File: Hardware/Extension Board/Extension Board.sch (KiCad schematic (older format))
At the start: 32 parts, among them J1 ARDUINO_COMMS, J10 CNX_MODE, J11 CNX_TUNING, J12 CNX_I2C, J13 CNX_I2C, J14 CNX_SPI, J15 CNX_SD, J16 CNX_TFT, J2 ARDUINO_DIGITAL, J3 ARDUINO_ANALOG, J4 CNX_LED, J5 CNX_LED, J6 CNX_LED, J7 CNX_LED, J8 CNX_SPARE, J9 CNX_NEXT_AGAIN, U1 74HC14

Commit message: PCB pour Extension board
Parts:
- removed J1: ARDUINO_COMMS, Connector_PinHeader_2.54mm:PinHeader_1x08_P2.54mm_Vertical, symbol Connector_Generic:Conn_01x08
- removed RN1: 10k, Resistor_THT:R_Array_SIP9, symbol Device:R_Network08
- added H1, H2: MountingHole, MountingHole:MountingHole_3.2mm_M3, symbol Mechanical:MountingHole
- added J7: ARDUINO_COMMS, Connector_PinHeader_2.54mm:PinHeader_1x06_P2.54mm_Vertical, symbol Connector_Generic:Conn_01x06
- added RN1: 10k, Resistor_THT:R_Array_SIP5, symbol Device:R_Network04
- C1, C2: footprint (none) -> Capacitor_THT:C_Rect_L7.2mm_W2.5mm_P5.00mm_FKS2_FKP2_MKS2_MKP2
- J1: renamed from J7; footprint MesModules:Bloc_de_jonction_CI-MPT_2.54mm_01x02 -> Connector_JST:JST_XH_B2B-XH-A_1x02_P2.50mm_Vertical
- J10, J12, J13: footprint Connector_JST:JST_EH_B4B-EH-A_1x04_P2.50mm_Vertical -> Connector_JST:JST_XH_B4B-XH-A_1x04_P2.50mm_Vertical
- J11, J9: footprint Connector_JST:JST_EH_B3B-EH-A_1x03_P2.50mm_Vertical -> Connector_JST:JST_XH_B3B-XH-A_1x03_P2.50mm_Vertical
- J14: footprint Connector_JST:JST_EH_B6B-EH-A_1x06_P2.50mm_Vertical -> Connector_JST:JST_XH_B6B-XH-AM_1x06_P2.50mm_Vertical
- J15: footprint Connector_JST:JST_EH_B4B-EH-A_1x04_P2.50mm_Vertical -> Connector_JST:JST_XH_B4B-XH-AM_1x04_P2.50mm_Vertical
- J16: footprint Connector_JST:JST_EH_B8B-EH-A_1x08_P2.50mm_Vertical -> Connector_JST:JST_XH_B8B-XH-AM_1x08_P2.50mm_Vertical
- J2: renamed from J6; footprint MesModules:Bloc_de_jonction_CI-MPT_2.54mm_01x02 -> Connector_JST:JST_XH_B2B-XH-A_1x02_P2.50mm_Vertical
- J3: renamed from J5; footprint MesModules:Bloc_de_jonction_CI-MPT_2.54mm_01x02 -> Connector_JST:JST_XH_B2B-XH-A_1x02_P2.50mm_Vertical
- J4: footprint MesModules:Bloc_de_jonction_CI-MPT_2.54mm_01x02 -> Connector_JST:JST_XH_B2B-XH-A_1x02_P2.50mm_Vertical
- J5: renamed from J8; footprint MesModules:Bloc_de_jonction_CI-MPT_2.54mm_01x03 -> Connector_JST:JST_XH_B3B-XH-A_1x03_P2.50mm_Vertical
- R1, R2, R3, R4, R5: value 220 -> 200; footprint (none) -> Resistor_THT:R_Axial_DIN0207_L6.3mm_D2.5mm_P10.16mm_Horizontal
- R10: value 20k -> 90k; footprint (none) -> Resistor_THT:R_Axial_DIN0207_L6.3mm_D2.5mm_P10.16mm_Horizontal
- R6: value 1M -> A CALCULER; footprint (none) -> Resistor_THT:R_Axial_DIN0411_L9.9mm_D3.6mm_P20.32mm_Horizontal
- R7, R8: footprint (none) -> Resistor_THT:R_Axial_DIN0207_L6.3mm_D2.5mm_P10.16mm_Horizontal
- R9: value 10k -> 50k; footprint (none) -> Resistor_THT:R_Axial_DIN0207_L6.3mm_D2.5mm_P10.16mm_Horizontal
- renumbered J2 to J6, J3 to J8
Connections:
- net labels added: D16, D17, D29, D31, D33, D40, D42, D48
- net labels removed: D27, D35, D41, D43, D49
- wire segments 154 -> 157
- no-connect marks 31 -> 25
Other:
- note added: "INPUTS\nwith ISR"
- note added: "PWM\nOUTPUTS"
- moved on the sheet: J13, J2, J4, J5, J8, R1, R2, R3, R4, R5

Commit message: PCB Extension board
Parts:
- J10: value CNX_MODE -> MODE
- J11: value CNX_TUNING -> TUNING
- J12, J13: value CNX_I2C -> I2C
- J14: value CNX_SPI -> SPI
- J15: value CNX_SD -> SD
- J16: value CNX_TFT -> TFT
- J5: value CNX_SPARE -> SPARE
- J9: value CNX_NEXT_AGAIN -> NEXT_AGAIN
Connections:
- net D18: now also U1.4; no longer U1.2
- net D19: now also U1.2; no longer U1.4
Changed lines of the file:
@@
 P 10400 1100
 F 0 "J11" H 10650 1000 50  0000 R CNN
-F 1 "CNX_TUNING" H 10950 1100 50  0000 R CNN
+F 1 "TUNING" H 10750 1100 50  0000 R CNN
 F 2 "Connector_JST:JST_XH_B3B-XH-A_1x03_P2.50mm_Vertical" H 10400 1100 50  0001 C CNN
 F 3 "~" H 10400 1100 50  0001 C CNN
@@
 P 6500 4250
 F 0 "J5" V 6750 4200 50  0000 L CNN
-F 1 "CNX_SPARE" V 6650 4050 50  0000 L CNN
+F 1 "SPARE" V 6650 4150 50  0000 L CNN
 F 2 "Connector_JST:JST_XH_B3B-XH-A_1x03_P2.50mm_Vertical" H 6500 4250 50  0001 C CNN
 F 3 "~" H 6500 4250 50  0001 C CNN
@@
 P 10150 2950
 F 0 "J13" H 10250 2750 50  0000 L CNN
-F 1 "CNX_I2C" H 10230 2851 50  0000 L CNN
+F 1 "I2C" H 10230 2851 50  0000 L CNN
 F 2 "Connector_JST:JST_XH_B4B-XH-A_1x04_P2.50mm_Vertical" H 10150 2950 50  0001 C CNN
 F 3 "~" H 10150 2950 50  0001 C CNN
@@
 Text GLabel 2550 3100 2    50   Input ~ 0
 D25
+Text GLabel 3650 5950 0    50   Input ~ 0
+D18
 Text GLabel 3650 5600 0    50   Input ~ 0
-D18
-Text GLabel 3650 5950 0    50   Input ~ 0
 D19
 Wire Wire Line
@@
 P 10150 4000
 F 0 "J14" H 10250 3700 50  0000 L CNN
-F 1 "CNX_SPI" H 10250 3800 50  0000 L CNN
+F 1 "SPI" H 10250 3800 50  0000 L CNN
 F 2 "Connector_JST:JST_XH_B6B-XH-AM_1x06_P2.50mm_Vertical" H 10150 4000 50  0001 C CNN
 F 3 "~" H 10150 4000 50  0001 C CNN
@@
 P 6800 5700
 F 0 "J9" H 6900 5700 50  0000 L CNN
-F 1 "CNX_NEXT_AGAIN" H 6900 5600 50  0000 L CNN
+F 1 "NEXT_AGAIN" H 6900 5600 50  0000 L CNN
 F 2 "Connector_JST:JST_XH_B3B-XH-A_1x03_P2.50mm_Vertical" H 6800 5700 50  0001 C CNN
 F 3 "~" H 6800 5700 50  0001 C CNN
@@
 P 8750 2950
 F 0 "J12" H 8850 2750 50  0000 L CNN
-F 1 "CNX_I2C" H 8830 2851 50  0000 L CNN
+F 1 "I2C" H 8830 2851 50  0000 L CNN
 F 2 "Connector_JST:JST_XH_B4B-XH-A_1x04_P2.50mm_Vertical" H 8750 2950 50  0001 C CNN
 F 3 "~" H 8750 2950 50  0001 C CNN
@@
 P 10350 5100
 F 0 "J15" H 10450 4900 50  0000 L CNN
-F 1 "CNX_SD" H 10430 5001 50  0000 L CNN
+F 1 "SD" H 10430 5001 50  0000 L CNN
 F 2 "Connector_JST:JST_XH_B4B-XH-AM_1x04_P2.50mm_Vertical" H 10350 5100 50  0001 C CNN
 F 3 "~" H 10350 5100 50  0001 C CNN
@@
 P 10350 5850
 F 0 "J16" H 10450 5450 50  0000 L CNN
-F 1 "CNX_TFT" H 10450 5550 50  0000 L CNN
+F 1 "TFT" H 10450 5550 50  0000 L CNN
 F 2 "Connector_JST:JST_XH_B8B-XH-AM_1x08_P2.50mm_Vertical" H 10350 5850 50  0001 C CNN
 F 3 "~" H 10350 5850 50  0001 C CNN
@@
 P 6350 1950
 F 0 "J10" H 6550 1750 50  0000 R CNN
-F 1 "CNX_MODE" H 6800 1850 50  0000 R CNN
+F 1 "MODE" H 6650 1850 50  0000 R CNN
 F 2 "Connector_JST:JST_XH_B4B-XH-A_1x04_P2.50mm_Vertical" H 6350 1950 50  0001 C CNN
 F 3 "~" H 6350 1950 50  0001 C CNN
@@
 P 1850 6200
 F 0 "J7" V 1814 6480 50  0000 L CNN
-F 1 "ARDUINO_COMMS" V 1723 6480 50  0000 L CNN
+F 1 "ARDUINO_COMMS" V 1950 5850 50  0000 L CNN
 F 2 "Connector_PinHeader_2.54mm:PinHeader_1x06_P2.54mm_Vertical" H 1850 6200 50  0001 C CNN
 F 3 "~" H 1850 6200 50  0001 C CNN

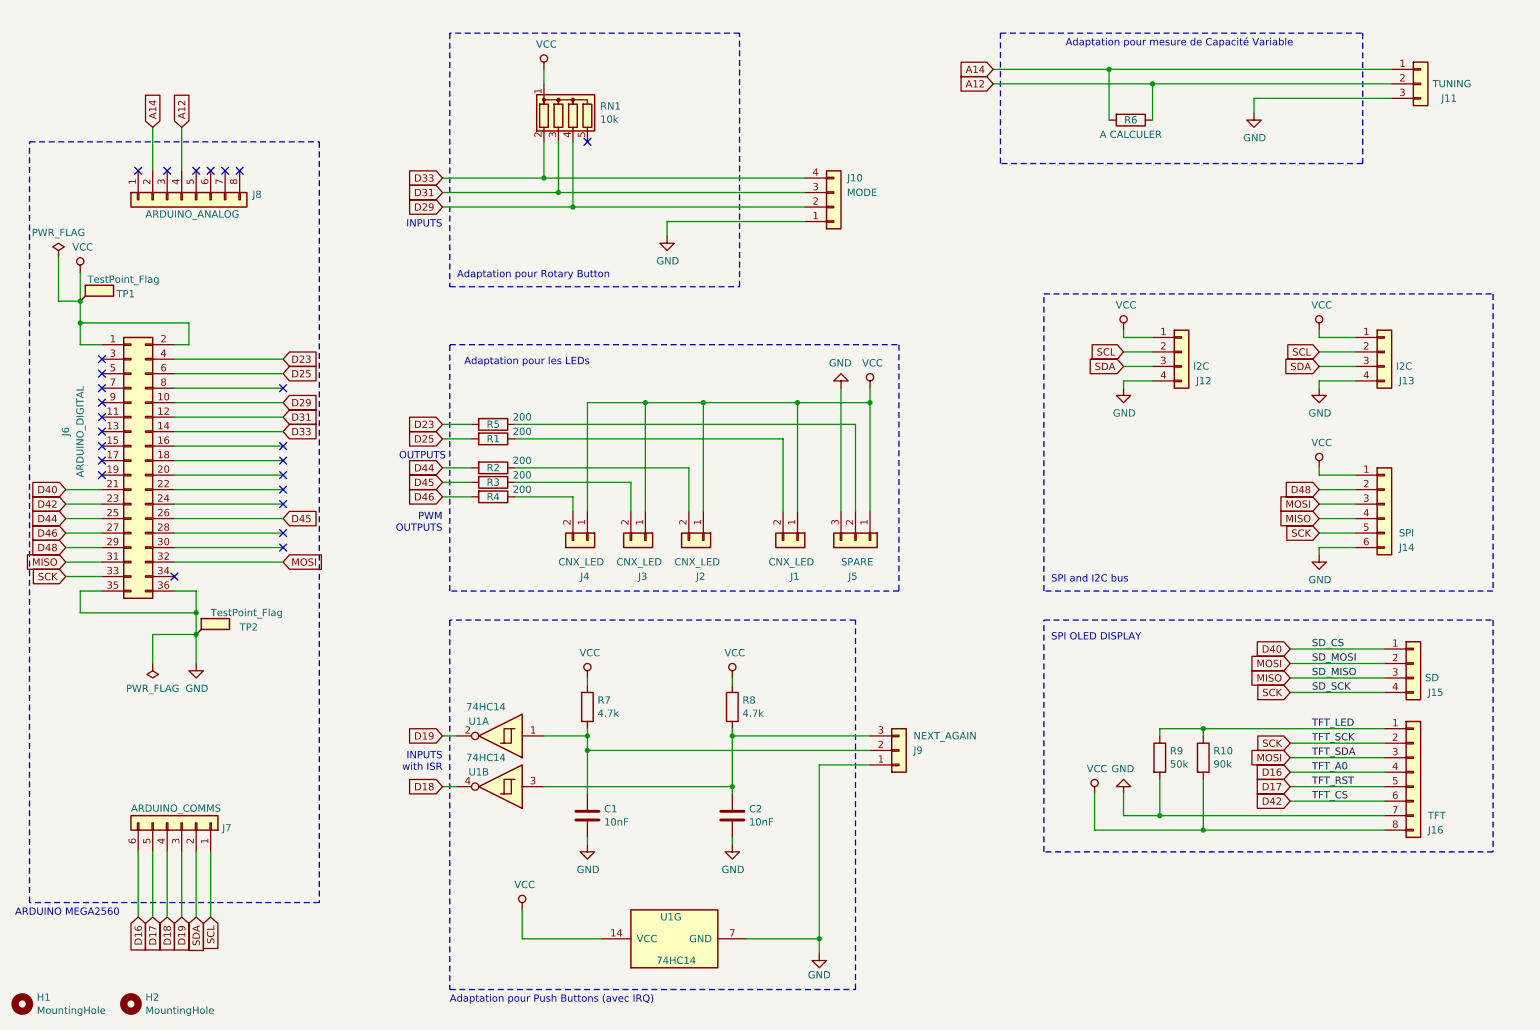
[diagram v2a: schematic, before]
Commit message: PCB Layout complete
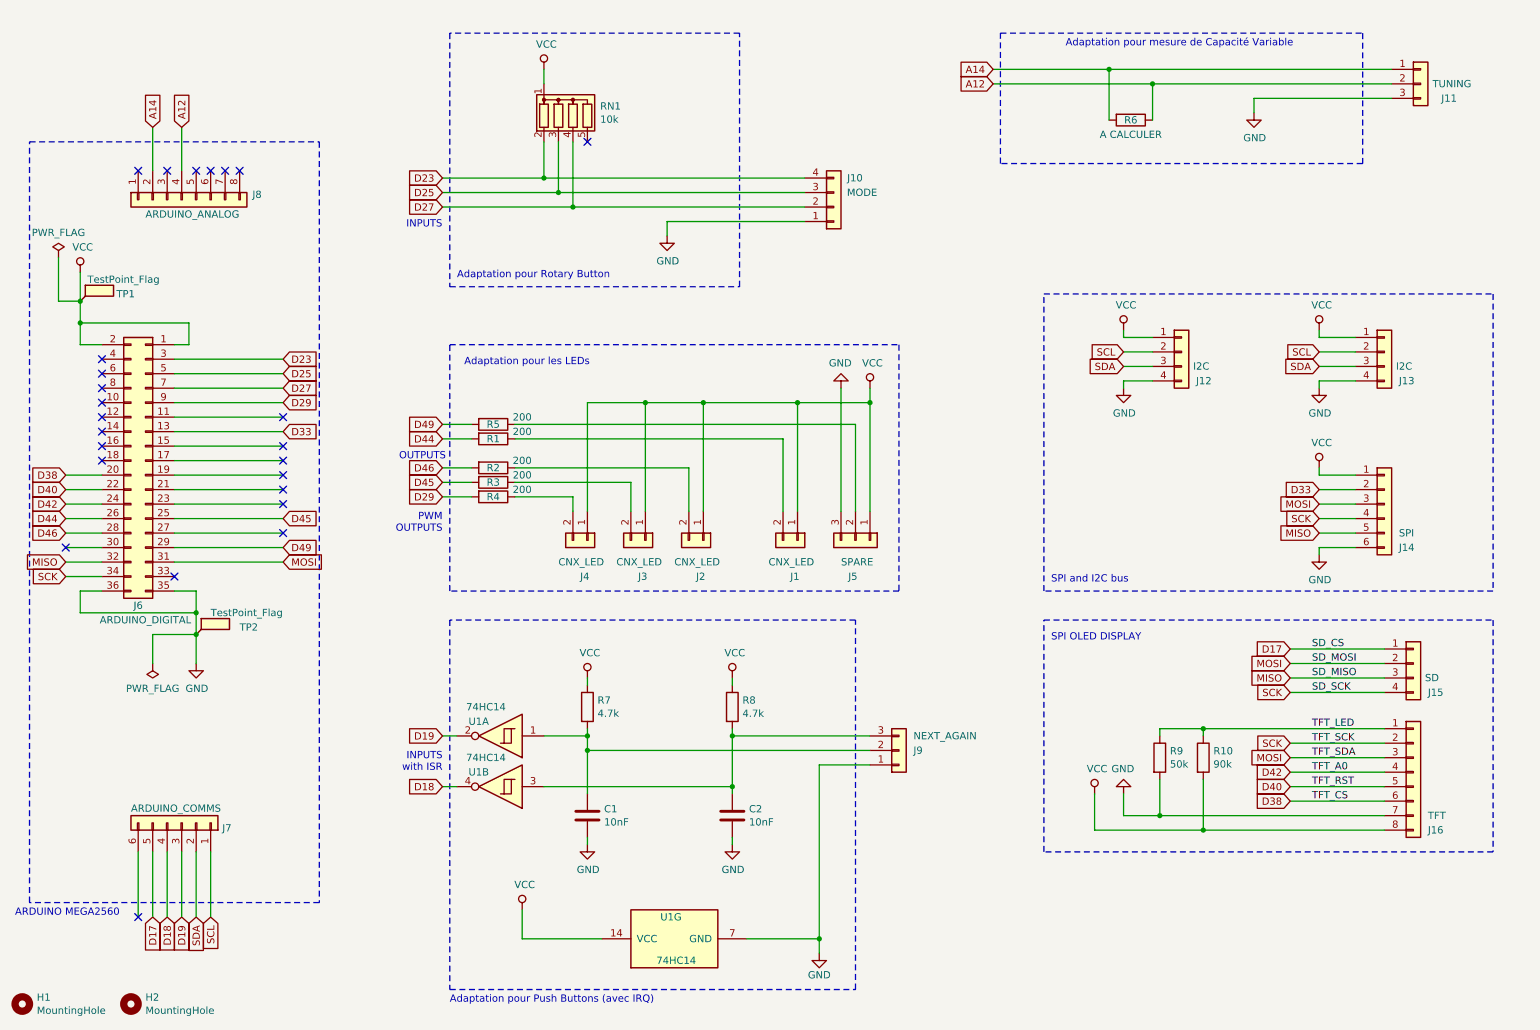
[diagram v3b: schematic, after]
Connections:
- net D17: now also J15.1 (Pin_1); no longer J16.5 (Pin_5)
- net D23: now also J10.4 (Pin_4), J6.3 (Pin_3), RN1.2 (R1); no longer J6.4 (Pin_4), R5.2
- net D25: now also J10.3 (Pin_3), J6.5 (Pin_5), RN1.3 (R2); no longer J6.6 (Pin_6), R1.2
- net D29: now also J6.9 (Pin_9), R4.2; no longer J10.2 (Pin_2), J6.10 (Pin_10), RN1.4 (R3)
- net D33: now also J14.2 (Pin_2), J6.13 (Pin_13); no longer J10.4 (Pin_4), J6.14 (Pin_14), RN1.2 (R1)
- net D40: now also J16.5 (Pin_5), J6.22 (Pin_22); no longer J15.1 (Pin_1), J6.21 (Pin_21)
- net D42: now also J16.4 (Pin_4), J6.24 (Pin_24); no longer J16.6 (Pin_6), J6.23 (Pin_23)
- net D44: now also J6.26 (Pin_26), R1.2; no longer J6.25 (Pin_25), R2.2
- net D45: now also J6.25 (Pin_25); no longer J6.26 (Pin_26)
- net D46: now also J6.28 (Pin_28), R2.2; no longer J6.27 (Pin_27), R4.2
- net MISO: now also J14.5 (Pin_5), J6.32 (Pin_32); no longer J14.4 (Pin_4), J6.31 (Pin_31)
- net MOSI: now also J6.31 (Pin_31); no longer J6.32 (Pin_32)
- net SCK: now also J14.4 (Pin_4), J6.34 (Pin_34); no longer J14.5 (Pin_5), J6.33 (Pin_33)
- net D38: now reaches J6.20 (Pin_20)
- net D38: now also J16.6 (Pin_6)
- net D27: now reaches J6.7 (Pin_7)
- net D27: now also J10.2 (Pin_2), RN1.4 (R3)
- net D16: no longer names the net of J7.6 (Pin_6)
- net D16: no longer J16.4 (Pin_4)
- removed net D31: J10.3 (Pin_3), J6.12 (Pin_12), RN1.3 (R2)
- net D48 renamed D49
- net D49: now also R5.2; no longer J14.2 (Pin_2)
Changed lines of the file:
@@
 	1800 4400 2550 4400
-Wire Wire Line
-	1050 4400 1300 4400
-Wire Wire Line
-	1050 4500 1300 4500
 Wire Wire Line
 	1950 4600 1800 4600
@@
 Wire Wire Line
 	1850 1700 1850 1400
-Text GLabel 9700 4100 0    50   Input ~ 0
+Text GLabel 9700 4200 0    50   Input ~ 0
 MISO
 Text GLabel 9700 4000 0    50   Input ~ 0
 MOSI
-Text GLabel 9700 4200 0    50   Input ~ 0
+Text GLabel 9700 4100 0    50   Input ~ 0
 SCK
 Wire Wire Line
@@
 	0    -1   -1   0
 $EndComp
-Text GLabel 2550 3000 2    50   Input ~ 0
-D23
-Text GLabel 2550 3100 2    50   Input ~ 0
-D25
+Text GLabel 2550 4300 2    50   Input ~ 0
+D49
+Text GLabel 2550 3500 2    50   Input ~ 0
+D33
 Text GLabel 3650 5950 0    50   Input ~ 0
 D18
@@
 	1    0    0    -1
 $EndComp
-Text GLabel 9700 3900 0    50   Input ~ 0
-D48
+Text GLabel 3650 3950 0    50   Input ~ 0
+D29
 $Comp
 L Connector_Generic:Conn_01x06 J14
@@
 NoConn ~ 1300 3200
 NoConn ~ 1300 3300
+NoConn ~ 1550 6850
 NoConn ~ 1300 3400
-NoConn ~ 1300 3500
-NoConn ~ 1300 3600
-NoConn ~ 1300 3700
-NoConn ~ 1300 3800
 NoConn ~ 1800 4500
-Wire Wire Line
-	1300 4600 1150 4600
 Wire Wire Line
 	1150 4600 1150 4750
@@
 Text GLabel 1050 4200 0    50   Input ~ 0
 D46
-Wire Wire Line
-	1050 4100 1300 4100
-Wire Wire Line
-	1050 4200 1300 4200
+Text GLabel 3650 3550 0    50   Input ~ 0
+D44
 Text GLabel 3650 3750 0    50   Input ~ 0
-D44
-Text GLabel 3650 3950 0    50   Input ~ 0
 D46
 Wire Wire Line
@@
 Wire Wire Line
 	1800 3800 2550 3800
-Text GLabel 1050 3900 0    50   Input ~ 0
-D40
+Text GLabel 1650 6850 3    50   Input ~ 0
+D17
 Wire Wire Line
 	1800 3900 2550 3900
@@
 	1800 4000 2550 4000
 NoConn ~ 4650 1500
-Text GLabel 3650 3550 0    50   Input ~ 0
-D25
+Text GLabel 9700 3900 0    50   Input ~ 0
+D33
 Text GLabel 3650 3450 0    50   Input ~ 0
-D23
+D49
 Wire Wire Line
 	3650 3450 3850 3450
@@
 	1150 2900 1150 2750
 Connection ~ 1150 2750
-Wire Wire Line
-	1150 2900 1300 2900
 Wire Wire Line
 	1150 2750 1900 2750
@@
 	8350 6150 8350 6000
 Text GLabel 9500 6050 0    50   Input ~ 0
-D42
+D38
 Wire Wire Line
 	10150 6050 9500 6050
@@
 	9500 5650 10150 5650
 Text GLabel 9500 5950 0    50   Input ~ 0
-D17
+D40
 Text GLabel 9500 5850 0    50   Input ~ 0
-D16
+D42
 Text Label 9650 5950 0    50   ~ 0
 TFT_RST
@@
 	9500 5200 10150 5200
 Text GLabel 9500 5000 0    50   Input ~ 0
-D40
+D17
 Wire Wire Line
 	9500 5300 10150 5300
@@
 Text Notes 7850 4550 0    50   ~ 0
 SPI and I2C bus
-Text GLabel 2550 3300 2    50   Input ~ 0
-D29
-Text GLabel 2550 3400 2    50   Input ~ 0
-D31
-Text GLabel 2550 3500 2    50   Input ~ 0
-D33
+Text GLabel 2550 3200 2    50   Input ~ 0
+D27
+Text GLabel 2550 3100 2    50   Input ~ 0
+D25
+Text GLabel 2550 3000 2    50   Input ~ 0
+D23
 Text GLabel 3650 1750 0    50   Input ~ 0
-D33
+D23
 Text GLabel 3650 1850 0    50   Input ~ 0
-D31
+D25
 Text GLabel 3650 1950 0    50   Input ~ 0
-D29
+D27
 Text Notes 3350 3700 0    50   ~ 0
 OUTPUTS
@@
 L Connector_Generic:Conn_02x18_Odd_Even J6
 U 1 1 5ED8EC88
-P 1500 3700
-F 0 "J6" V 1050 3900 50  0000 C CNN
-F 1 "ARDUINO_DIGITAL" V 1150 3900 50  0000 C CNN
-F 2 "Connector_PinHeader_2.54mm:PinHeader_2x18_P2.54mm_Vertical" H 1500 3700 50  0001 C CNN
-F 3 "~" H 1500 3700 50  0001 C CNN
-	1    1500 3700
-	1    0    0    -1
-$EndComp
-Text GLabel 1050 4300 0    50   Input ~ 0
-D48
-Wire Wire Line
-	1050 4300 1300 4300
+P 1600 3700
+F 0 "J6" H 1650 2700 50  0000 C CNN
+F 1 "ARDUINO_DIGITAL" H 1600 2600 50  0000 C CNN
+F 2 "Connector_PinHeader_2.54mm:PinHeader_2x18_P2.54mm_Vertical" H 1600 3700 50  0001 C CNN
+F 3 "~" H 1600 3700 50  0001 C CNN
+	1    1600 3700
+	-1   0    0    -1
+$EndComp
+Text GLabel 2550 3300 2    50   Input ~ 0
+D29
 $Comp
 L Connector_Generic:Conn_01x06 J7
@@
 	0    1    -1   0
 $EndComp
-NoConn ~ 2550 4300
-Text GLabel 1550 6850 3    50   Input ~ 0
-D16
-Wire Wire Line
-	1550 6400 1550 6850
-Text GLabel 1650 6850 3    50   Input ~ 0
-D17
-Wire Wire Line
-	1650 6400 1650 6850
 Text GLabel 1050 4000 0    50   Input ~ 0
 D42
 Wire Wire Line
-	1050 4000 1300 4000
-Wire Wire Line
-	1050 3900 1300 3900
+	1550 6400 1550 6850
+Text GLabel 1050 3900 0    50   Input ~ 0
+D40
+Wire Wire Line
+	1650 6400 1650 6850
 NoConn ~ 2550 3900
 Wire Wire Line
@@
 	1    0    0    -1
 $EndComp
-NoConn ~ 2550 3200
+NoConn ~ 2550 4000
+NoConn ~ 1050 4300
+NoConn ~ 1300 3700
+Wire Wire Line
+	1050 4000 1300 4000
+Wire Wire Line
+	1050 3900 1300 3900
+Wire Wire Line
+	1050 4100 1300 4100
+Wire Wire Line
+	1050 4200 1300 4200
+Wire Wire Line
+	1050 4300 1300 4300
+Wire Wire Line
+	1050 4400 1300 4400
+Wire Wire Line
+	1050 4500 1300 4500
+Wire Wire Line
+	1150 4600 1300 4600
+NoConn ~ 1300 3500
+Wire Wire Line
+	1150 2900 1300 2900
+NoConn ~ 1300 3600
+Wire Wire Line
+	1300 3800 1050 3800
 NoConn ~ 2550 3600
-NoConn ~ 2550 4000
+NoConn ~ 2550 3400
+Text GLabel 1050 3800 0    50   Input ~ 0
+D38
 $EndSCHEMATC

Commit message: PCB updated.
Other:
- note added: "PWM"
- note removed: "PWM\nOUTPUTS"
- moved on the sheet: R1
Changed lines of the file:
@@
 	1800 3300 2550 3300
-Wire Wire Line
-	1800 3400 2550 3400
 Wire Wire Line
 	1800 3500 2550 3500
@@
 L Device:R R1
 U 1 1 5EDB077A
-P 4000 3550
-F 0 "R1" V 4000 3550 50  0000 C CNN
-F 1 "200" V 3950 3750 50  0000 C CNN
-F 2 "Resistor_THT:R_Axial_DIN0207_L6.3mm_D2.5mm_P10.16mm_Horizontal" V 3930 3550 50  0001 C CNN
-F 3 "~" H 4000 3550 50  0001 C CNN
-	1    4000 3550
+P 4000 3650
+F 0 "R1" V 4000 3650 50  0000 C CNN
+F 1 "200" V 3950 3850 50  0000 C CNN
+F 2 "Resistor_THT:R_Axial_DIN0207_L6.3mm_D2.5mm_P10.16mm_Horizontal" V 3930 3650 50  0001 C CNN
+F 3 "~" H 4000 3650 50  0001 C CNN
+	1    4000 3650
 	0    1    1    0
 $EndComp
@@
 $EndComp
 Wire Wire Line
-	4150 3550 6000 3550
-Wire Wire Line
-	6000 3550 6000 4050
+	4150 3650 6000 3650
+Wire Wire Line
+	6000 3650 6000 4050
 Wire Wire Line
 	4150 3750 5350 3750
@@
 Wire Wire Line
 	1800 4300 2550 4300
-Wire Wire Line
-	1800 4200 2550 4200
 Text GLabel 2550 4100 2    50   Input ~ 0
 D45
@@
 NoConn ~ 1300 3200
 NoConn ~ 1300 3300
-NoConn ~ 1550 6850
+NoConn ~ 1550 6400
 NoConn ~ 1300 3400
 NoConn ~ 1800 4500
@@
 Text GLabel 1050 4200 0    50   Input ~ 0
 D46
-Text GLabel 3650 3550 0    50   Input ~ 0
+Text GLabel 3650 3650 0    50   Input ~ 0
 D44
 Text GLabel 3650 3750 0    50   Input ~ 0
@@
 Wire Wire Line
 	3650 3850 3850 3850
-Wire Wire Line
-	1800 3600 2550 3600
-Wire Wire Line
-	1800 3700 2550 3700
-Wire Wire Line
-	1800 3800 2550 3800
 Text GLabel 1650 6850 3    50   Input ~ 0
 D17
-Wire Wire Line
-	1800 3900 2550 3900
-Wire Wire Line
-	1800 4000 2550 4000
 NoConn ~ 4650 1500
 Text GLabel 9700 3900 0    50   Input ~ 0
@@
 	3650 3450 3850 3450
 Wire Wire Line
-	3650 3550 3850 3550
+	3650 3650 3850 3650
 Wire Wire Line
 	1150 2900 1150 2750
@@
 Text Notes 3650 5850 2    50   ~ 0
 INPUTS\nwith ISR
-Text Notes 3650 4200 2    50   ~ 0
-PWM\nOUTPUTS
+Text Notes 3450 3700 2    50   ~ 0
+PWM
 Text Notes 3400 2100 0    50   ~ 0
 INPUTS
@@
 Wire Wire Line
 	9700 3800 9950 3800
-NoConn ~ 2550 3700
-NoConn ~ 2550 3800
-NoConn ~ 2550 4200
+NoConn ~ 1800 3700
+NoConn ~ 1800 3800
+NoConn ~ 1800 4200
 $Comp
 L power:PWR_FLAG #FLG0101
@@
 Text GLabel 3650 1950 0    50   Input ~ 0
 D27
-Text Notes 3350 3700 0    50   ~ 0
+Text Notes 3400 4100 0    50   ~ 0
 OUTPUTS
 $Comp
@@
 Text GLabel 1050 4000 0    50   Input ~ 0
 D42
-Wire Wire Line
-	1550 6400 1550 6850
 Text GLabel 1050 3900 0    50   Input ~ 0
 D40
 Wire Wire Line
 	1650 6400 1650 6850
-NoConn ~ 2550 3900
+NoConn ~ 1800 3900
 Wire Wire Line
 	5650 5550 5650 5600
@@
 	1    0    0    -1
 $EndComp
-NoConn ~ 2550 4000
-NoConn ~ 1050 4300
+NoConn ~ 1800 4000
+NoConn ~ 1300 4300
 NoConn ~ 1300 3700
 Wire Wire Line
@@
 Wire Wire Line
 	1050 4200 1300 4200
-Wire Wire Line
-	1050 4300 1300 4300
 Wire Wire Line
 	1050 4400 1300 4400
@@
 Wire Wire Line
 	1300 3800 1050 3800
-NoConn ~ 2550 3600
-NoConn ~ 2550 3400
+NoConn ~ 1800 3600
+NoConn ~ 1800 3400
 Text GLabel 1050 3800 0    50   Input ~ 0
 D38
+Text Notes 3450 3800 2    50   ~ 0
+PWM
+Text Notes 3450 3900 2    50   ~ 0
+PWM
 $EndSCHEMATC
